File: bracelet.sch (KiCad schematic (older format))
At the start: 43 parts

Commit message: Added charging and fuel gage circuit
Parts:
- removed C?: 1uF, symbol Device:C
- removed C?: 0.47uF, symbol Device:C
- removed C? (x2): 4.7uF, symbol Device:C
- removed R?: 0.010, symbol Device:R
- removed R? (x4): 5.1k, symbol Device:R
- removed R? (x2): 10k, symbol Device:R
- removed U?: BQ27441-G1, Package_SON:Texas_S-PDSO-N12, symbol Battery_Management:BQ27441-G1
- removed U?: MCP73831-2-OT, Package_TO_SOT_SMD:SOT-23-5, symbol Battery_Management:MCP73831-2-OT
- added C? (x2): 4.7uF, symbol Device:C
- added C?: 1uF, symbol Device:C
- added C?: 2.2uF, symbol Device:C
- added IC?: MCP73811T-420I_OT, SOT95P270X145-5N, symbol Battery_Charger:MCP73811T-420I_OT
- added IC?: BQ27426YZFR, BGA9C50P3X3_158X162X62, symbol Fuel_Gage:BQ27426YZFR
- added R?: 0.01, symbol Device:R_US
- added R? (x4): 10k, symbol Device:R_US
- J?: value Battery 100mAh -> Battery_175mAh
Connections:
- net labels added: VCC_VIN_USB, V_BAT
- net labels removed: VSYS
- wire segments 196 -> 189
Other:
- moved on the sheet: C?, D?, IC?, J?, L?, R?

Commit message: Finished Battery Management Circuit Rough Draft
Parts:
- removed D?: D_Schottky, symbol Device:D_Schottky
- removed J?: Conn_01x06_Female, symbol Connector:Conn_01x06_Female
- added C?: 1uF, symbol Device:C
- added D?: D_Schottky, symbol Device:D_Schottky
- added Q?: Q_PMOS_DSG, symbol Device:Q_PMOS_DSG
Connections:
- net labels added: VCC_3V8, VCC_SYS
- net labels removed: STAT, VCC_5V, VCC_VIN_USB, V_BAT
- wire segments 189 -> 181
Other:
- moved on the sheet: C?, D?, IC?, J?, R?

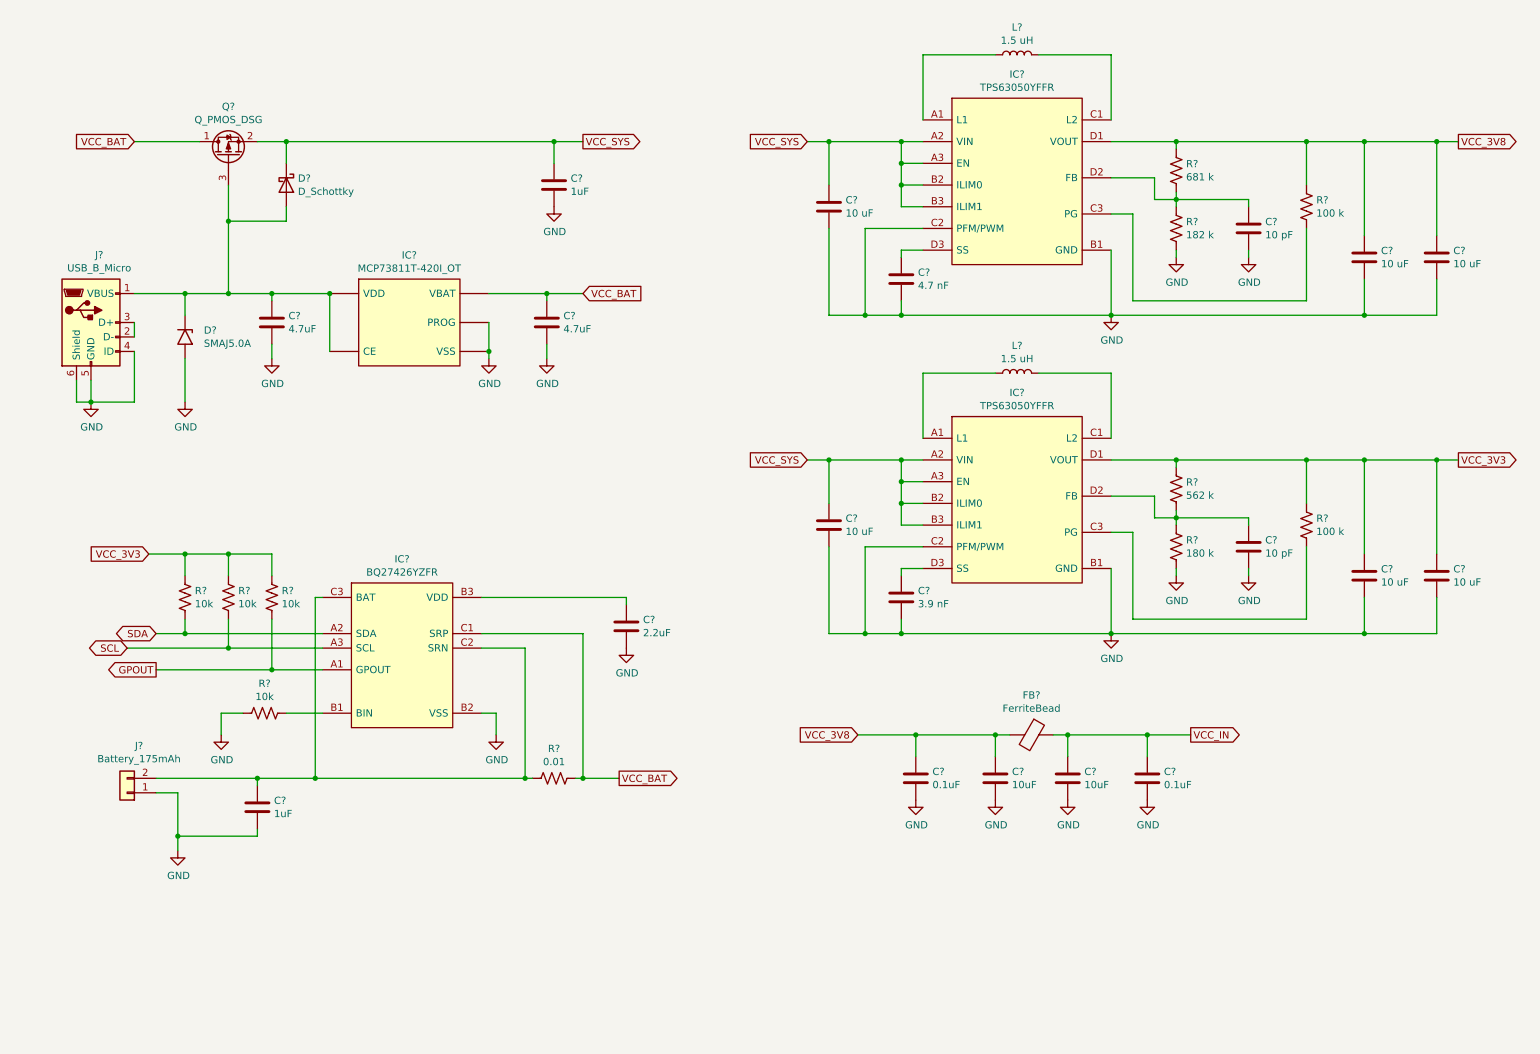
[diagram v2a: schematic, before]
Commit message: Added hierarchical sheets and the 60 pin connector
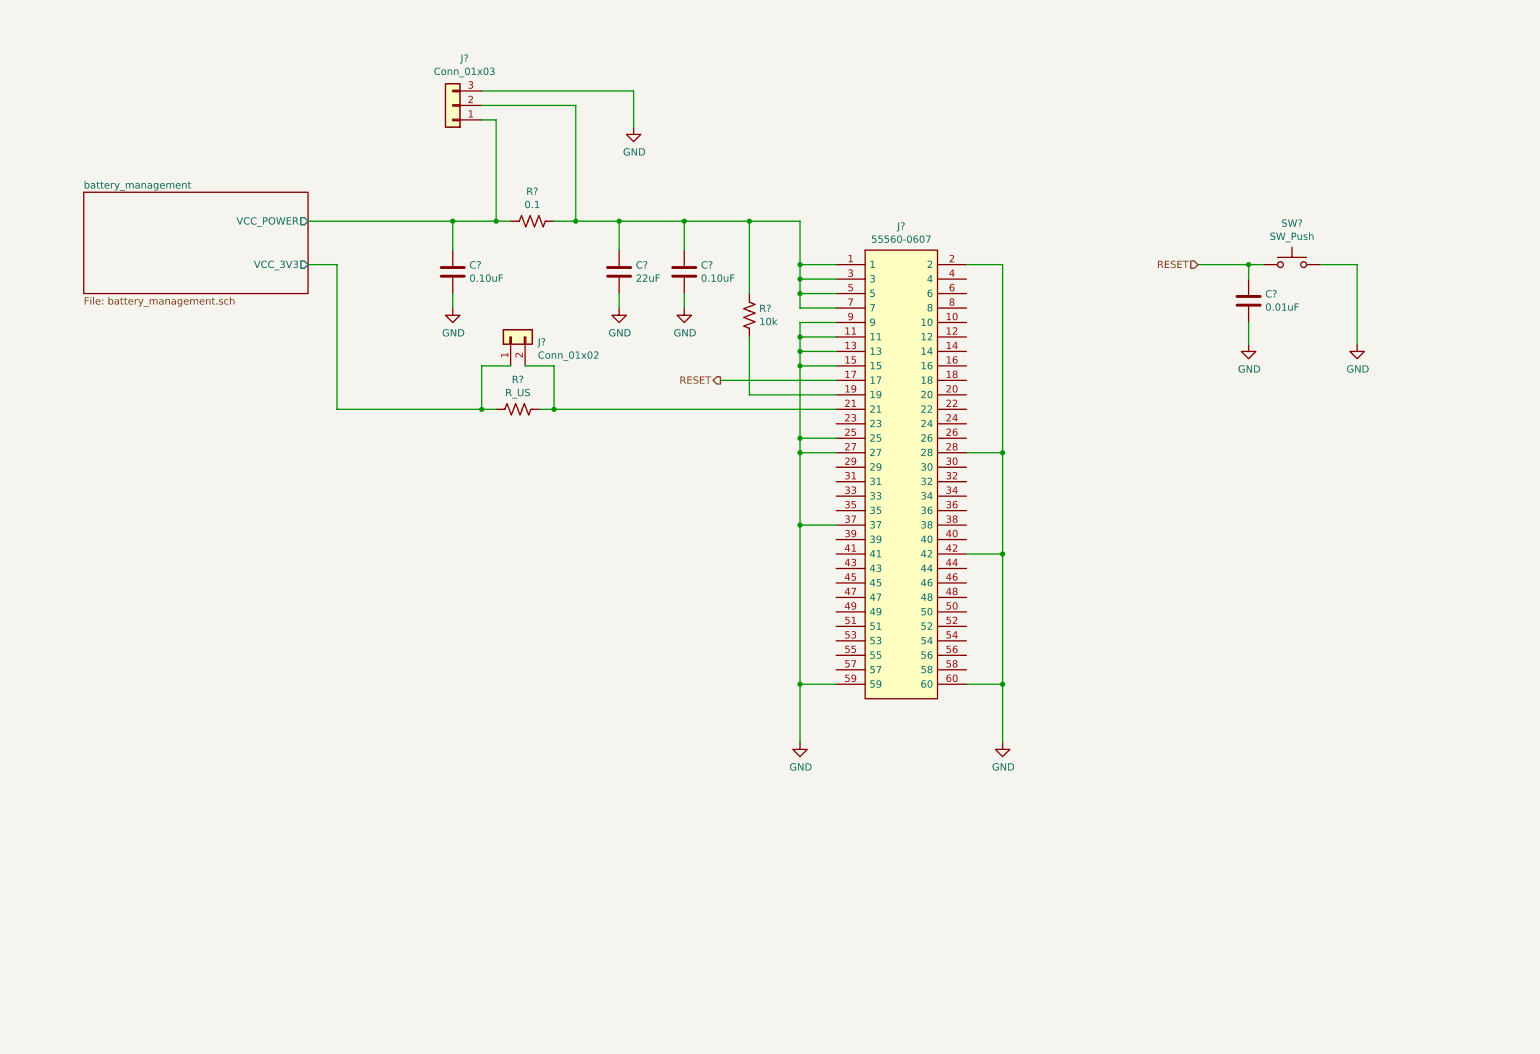
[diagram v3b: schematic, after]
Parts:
- removed C? (x2): 4.7uF, symbol Device:C
- removed C? (x2): 1uF, symbol Device:C
- removed C?: 2.2uF, symbol Device:C
- removed C? (x2): 0.1uF, symbol Device:C
- removed C? (x2): 10uF, symbol Device:C
- removed C? (x6): 10 uF, symbol Device:C
- removed C?: 4.7 nF, symbol Device:C
- removed C?: 3.9 nF, symbol Device:C
- removed C? (x2): 10 pF, symbol Device:C
- removed D?: D_Schottky, symbol Device:D_Schottky
- removed D?: SMAJ5.0A, DIOM5026X229N, symbol Diode_TVS:SMAJ5.0A
- removed FB?: FerriteBead, symbol Device:FerriteBead
- removed IC?: MCP73811T-420I_OT, SOT95P270X145-5N, symbol Battery_Charger:MCP73811T-420I_OT
- removed IC?: BQ27426YZFR, BGA9C50P3X3_158X162X62, symbol Fuel_Gage:BQ27426YZFR
- removed IC? (x2): TPS63050YFFR, BGA12C40P3X4_129X169X62, symbol Buck_Boost_Converter:TPS63050YFFR
- removed J?: USB_B_Micro, symbol Connector:USB_B_Micro
- removed J?: Battery_175mAh, symbol Connector_Generic:Conn_01x02
- removed L? (x2): 1.5 uH, symbol Device:L
- removed Q?: Q_PMOS_DSG, symbol Device:Q_PMOS_DSG
- removed R?: 0.01, symbol Device:R_US
- removed R? (x4): 10k, symbol Device:R_US
- removed R?: 681 k, symbol Device:R_US
- removed R?: 182 k, symbol Device:R_US
- removed R? (x2): 100 k, symbol Device:R_US
- removed R?: 562 k, symbol Device:R_US
- removed R?: 180 k, symbol Device:R_US
- added C?: 22uF, symbol Device:C
- added C? (x2): 0.10uF, symbol Device:C
- added C?: 0.01uF, symbol Device:C
- added J?: 55560-0607, 555600607, symbol Connector_60PIN:55560-0607
- added J?: Conn_01x03, symbol Connector_Generic:Conn_01x03
- added J?: Conn_01x02, symbol Connector_Generic:Conn_01x02
- added R?: 10k, symbol Device:R_US
- added R?: 0.1, symbol Device:R_US
- added R?: R_US, symbol Device:R_US
- added SW?: SW_Push, symbol Switch:SW_Push
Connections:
- net GND: now also C?.2, C?.2, C?.2, C?.2, J?.11, J?.13, J?.15, J?.2, J?.25, J?.27, J?.28, J?.3 (Pin_3), J?.37, J?.42, J?.59, J?.60, J?.9, SW?.2
- new net: C?.1, C?.1, J?.1, J?.2 (Pin_2), J?.3, J?.5, J?.7, R?.1, R?.1
- new net: J?.19, R?.2
- new net: J?.2 (Pin_2), J?.21, R?.1
- new net RESET: C?.1, J?.17, SW?.1
- new net battery_management/VCC_3V3: J?.1 (Pin_1), R?.2
- new net battery_management/VCC_POWER: C?.1, J?.1 (Pin_1), R?.2

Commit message: Finally finished final draft
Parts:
- added J2: Conn_01x08, symbol Connector_Generic:Conn_01x08
- added J3: Conn_01x06, symbol Connector_Generic:Conn_01x06
- gave numbers to parts that had none: 7
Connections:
- net IO5_DFU: now reaches J1.10
- net IO5_DFU: now also J3.4 (Pin_4)
- net IO12_BM_GPOUT: now reaches J1.24
- net IO12_BM_GPOUT: now also J3.1 (Pin_1)
- net IO30_BM_SDA: now reaches J1.30
- net IO30_BM_SDA: now also J3.2 (Pin_2)
- net IO31_BM_SCL: now reaches J1.32
- net IO31_BM_SCL: now also J3.3 (Pin_3)
- net IO0_UART1_RX: now reaches J1.44
- net IO0_UART1_RX: now also J2.1 (Pin_1)
- net IO1_UART1_TX: now reaches J1.46
- net IO1_UART1_TX: now also J2.2 (Pin_2)
- net IO14_UART1_RTS: now reaches J1.48
- net IO14_UART1_RTS: now also J2.3 (Pin_3)
- net IO15_UART1_CTS: now reaches J1.50
- net IO15_UART1_CTS: now also J2.4 (Pin_4)
- net IO28_UART0_RX: now reaches J1.52
- net IO28_UART0_RX: now also J2.5 (Pin_5)
- net IO29_UART0_TX: now reaches J1.54
- net IO29_UART0_TX: now also J2.6 (Pin_6)
- net SWDIO: now reaches J1.55
- net SWDIO: now also J3.5 (Pin_5)
- net IO27_UART0_RTS: now reaches J1.56
- net IO27_UART0_RTS: now also J2.7 (Pin_7)
- net SWDCLK: now reaches J1.57
- net SWDCLK: now also J3.6 (Pin_6)
- net IO26_UART0_CTS: now reaches J1.58
- net IO26_UART0_CTS: now also J2.8 (Pin_8)
- no-connect marks 0 -> 27
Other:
- moved on the sheet: C?, SW1

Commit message: Fixed some symbols, assigned some footprints, and made wire labels
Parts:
- J3: renamed from J1; footprint 555600607 -> Connector_Skywire:555600607
- gave numbers to parts that had none: 4
- renumbered C3 to C1, C1 to C3, J4 to J1, J5 to J2, J3 to J4, J2 to J5

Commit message: Chose more parts and added more footprints. Have some resistors and all the capacitors to go
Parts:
- removed SW1: SW_Push, symbol Switch:SW_Push
- added SW1: KMR231GLFS, Button_Switch_SMD:KMR2_1, symbol Button_Switch:KMR231GLFS
- J1: footprint (none) -> Connector_PinHeader_2.54mm:PinHeader_1x03_P2.54mm_Vertical
- J2: footprint (none) -> Connector_PinSocket_2.54mm:PinSocket_1x02_P2.54mm_Vertical
- J4: footprint (none) -> Connector_PinSocket_2.54mm:PinSocket_1x06_P2.54mm_Vertical
- J5: footprint (none) -> Connector_PinSocket_2.54mm:PinSocket_1x08_P2.54mm_Vertical
- R1: value R_US -> 0.1; footprint (none) -> Resistor_SMD:R_0805_2012Metric
- R2: footprint (none) -> Resistor_SMD:R_0805_2012Metric
- R3: footprint (none) -> Resistor_SMD:R_0402_1005Metric
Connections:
- no-connect marks 27 -> 29
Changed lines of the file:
@@
 F 0 "J1" H 3518 875 50  0000 C CNN
 F 1 "Conn_01x03" H 3518 966 50  0000 C CNN
-F 2 "" H 3600 1200 50  0001 C CNN
+F 2 "Connector_PinHeader_2.54mm:PinHeader_1x03_P2.54mm_Vertical" H 3600 1200 50  0001 C CNN
 F 3 "~" H 3600 1200 50  0001 C CNN
 	1    3600 1200
@@
 F 0 "R3" H 5718 2696 50  0000 L CNN
 F 1 "10k" H 5718 2605 50  0000 L CNN
-F 2 "" V 5690 2640 50  0001 C CNN
+F 2 "Resistor_SMD:R_0402_1005Metric" V 5690 2640 50  0001 C CNN
 F 3 "~" H 5650 2650 50  0001 C CNN
 	1    5650 2650
@@
 F 0 "R2" V 3945 2000 50  0000 C CNN
 F 1 "0.1" V 4036 2000 50  0000 C CNN
-F 2 "" V 4190 1990 50  0001 C CNN
+F 2 "Resistor_SMD:R_0805_2012Metric" V 4190 1990 50  0001 C CNN
 F 3 "~" H 4150 2000 50  0001 C CNN
 	1    4150 2000
@@
 Wire Wire Line
 	4300 2000 4450 2000
-$Comp
-L Switch:SW_Push SW1
-U 1 1 60CE0377
-P 9800 1400
-F 0 "SW1" H 9800 1685 50  0000 C CNN
-F 1 "SW_Push" H 9800 1594 50  0000 C CNN
-F 2 "" H 9800 1600 50  0001 C CNN
-F 3 "~" H 9800 1600 50  0001 C CNN
-	1    9800 1400
-	1    0    0    -1
-$EndComp
 Wire Wire Line
 	9600 1400 9500 1400
@@
 $EndComp
 Wire Wire Line
-	10000 1400 10250 1400
-Wire Wire Line
-	10250 1400 10250 1950
+	10400 1400 10650 1400
+Wire Wire Line
+	10650 1400 10650 1950
 $Comp
 L power:GND #PWR08
 U 1 1 60CE59B3
-P 10250 1950
-F 0 "#PWR08" H 10250 1700 50  0001 C CNN
-F 1 "GND" H 10255 1777 50  0000 C CNN
-F 2 "" H 10250 1950 50  0001 C CNN
-F 3 "" H 10250 1950 50  0001 C CNN
-	1    10250 1950
+P 10650 1950
+F 0 "#PWR08" H 10650 1700 50  0001 C CNN
+F 1 "GND" H 10655 1777 50  0000 C CNN
+F 2 "" H 10650 1950 50  0001 C CNN
+F 3 "" H 10650 1950 50  0001 C CNN
+	1    10650 1950
 	1    0    0    -1
 $EndComp
@@
 F 0 "J2" V 3964 2612 50  0000 R CNN
 F 1 "Conn_01x02" V 3873 2612 50  0000 R CNN
-F 2 "" H 4000 2800 50  0001 C CNN
+F 2 "Connector_PinSocket_2.54mm:PinSocket_1x02_P2.54mm_Vertical" H 4000 2800 50  0001 C CNN
 F 3 "~" H 4000 2800 50  0001 C CNN
 	1    4000 2800
@@
 P 4050 3300
 F 0 "R1" V 3845 3300 50  0000 C CNN
-F 1 "R_US" V 3936 3300 50  0000 C CNN
-F 2 "" V 4090 3290 50  0001 C CNN
+F 1 "0.1" V 3936 3300 50  0000 C CNN
+F 2 "Resistor_SMD:R_0805_2012Metric" V 4090 3290 50  0001 C CNN
 F 3 "~" H 4050 3300 50  0001 C CNN
 	1    4050 3300
@@
 F 0 "J5" H 10430 4692 50  0000 L CNN
 F 1 "Conn_01x08" H 10430 4601 50  0000 L CNN
-F 2 "" H 10350 4700 50  0001 C CNN
+F 2 "Connector_PinSocket_2.54mm:PinSocket_1x08_P2.54mm_Vertical" H 10350 4700 50  0001 C CNN
 F 3 "~" H 10350 4700 50  0001 C CNN
 	1    10350 4700
@@
 F 0 "J4" H 10430 3292 50  0000 L CNN
 F 1 "Conn_01x06" H 10430 3201 50  0000 L CNN
-F 2 "" H 10350 3300 50  0001 C CNN
+F 2 "Connector_PinSocket_2.54mm:PinSocket_1x06_P2.54mm_Vertical" H 10350 3300 50  0001 C CNN
 F 3 "~" H 10350 3300 50  0001 C CNN
 	1    10350 3300
@@
 Text Label 9400 5100 0    50   ~ 0
 IO26_UART0_CTS
+$Comp
+L Button_Switch:KMR231GLFS SW1
+U 1 1 6076F590
+P 10000 1350
+F 0 "SW1" H 10000 1665 50  0000 C CNN
+F 1 "KMR231GLFS" H 10000 1574 50  0000 C CNN
+F 2 "Button_Switch_SMD:KMR2_1" H 9850 1050 50  0001 L CNN
+F 3 "https://componentsearchengine.com/Datasheets/1/KMR231GLFS.pdf" H 9850 950 50  0001 L CNN
+F 4 "Tactile Switches Spst-No 300Gf Gw Smd" H 9850 850 50  0001 L CNN "Description"
+F 5 "C & K COMPONENTS" H 9850 650 50  0001 L CNN "Manufacturer_Name"
+F 6 "KMR231GLFS" H 9850 550 50  0001 L CNN "Manufacturer_Part_Number"
+F 7 "611-KMR231GLFS" H 9850 450 50  0001 L CNN "Mouser Part Number"
+F 8 "https://www.mouser.co.uk/ProductDetail/CK/KMR231GLFS?qs=sb%252But3Lm4x27Wura%2FoX2iQ%3D%3D" H 9850 350 50  0001 L CNN "Mouser Price/Stock"
+F 9 "KMR231GLFS" H 9850 250 50  0001 L CNN "Arrow Part Number"
+F 10 "https://www.arrow.com/en/products/kmr231glfs/ck" H 9850 150 50  0001 L CNN "Arrow Price/Stock"
+	1    10000 1350
+	1    0    0    -1
+$EndComp
+NoConn ~ 10400 1300
+NoConn ~ 9600 1300
 $EndSCHEMATC

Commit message: Finished assigning footprints, and generated netlist
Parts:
- C1, C3: value 0.10uF -> 0.1uF; footprint (none) -> Capacitor_SMD:C_0603_1608Metric
- C2: footprint (none) -> Capacitor_SMD:C_1210_3225Metric
- C4: footprint (none) -> Capacitor_SMD:C_0603_1608Metric
- R3: footprint Resistor_SMD:R_0402_1005Metric -> Resistor_SMD:R_1206_3216Metric
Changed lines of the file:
@@
 F 0 "R3" H 5718 2696 50  0000 L CNN
 F 1 "10k" H 5718 2605 50  0000 L CNN
-F 2 "Resistor_SMD:R_0402_1005Metric" V 5690 2640 50  0001 C CNN
+F 2 "Resistor_SMD:R_1206_3216Metric" V 5690 2640 50  0001 C CNN
 F 3 "~" H 5650 2650 50  0001 C CNN
 	1    5650 2650
@@
 F 0 "C2" H 4865 2396 50  0000 L CNN
 F 1 "22uF" H 4865 2305 50  0000 L CNN
-F 2 "" H 4788 2200 50  0001 C CNN
+F 2 "Capacitor_SMD:C_1210_3225Metric" H 4788 2200 50  0001 C CNN
 F 3 "~" H 4750 2350 50  0001 C CNN
 	1    4750 2350
@@
 F 0 "C4" H 9615 1696 50  0000 L CNN
 F 1 "0.01uF" H 9615 1605 50  0000 L CNN
-F 2 "" H 9538 1500 50  0001 C CNN
+F 2 "Capacitor_SMD:C_0603_1608Metric" H 9538 1500 50  0001 C CNN
 F 3 "~" H 9500 1650 50  0001 C CNN
 	1    9500 1650
@@
 P 3600 2350
 F 0 "C1" H 3715 2396 50  0000 L CNN
-F 1 "0.10uF" H 3715 2305 50  0000 L CNN
-F 2 "" H 3638 2200 50  0001 C CNN
+F 1 "0.1uF" H 3715 2305 50  0000 L CNN
+F 2 "Capacitor_SMD:C_0603_1608Metric" H 3638 2200 50  0001 C CNN
 F 3 "~" H 3600 2350 50  0001 C CNN
 	1    3600 2350
@@
 P 5200 2350
 F 0 "C3" H 5315 2396 50  0000 L CNN
-F 1 "0.10uF" H 5315 2305 50  0000 L CNN
-F 2 "" H 5238 2200 50  0001 C CNN
+F 1 "0.1uF" H 5315 2305 50  0000 L CNN
+F 2 "Capacitor_SMD:C_0603_1608Metric" H 5238 2200 50  0001 C CNN
 F 3 "~" H 5200 2350 50  0001 C CNN
 	1    5200 2350
